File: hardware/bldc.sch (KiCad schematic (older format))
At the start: 7 parts, among them J3 U_OUT, J4 V_OUT, J5 W_OUT, U1 7805

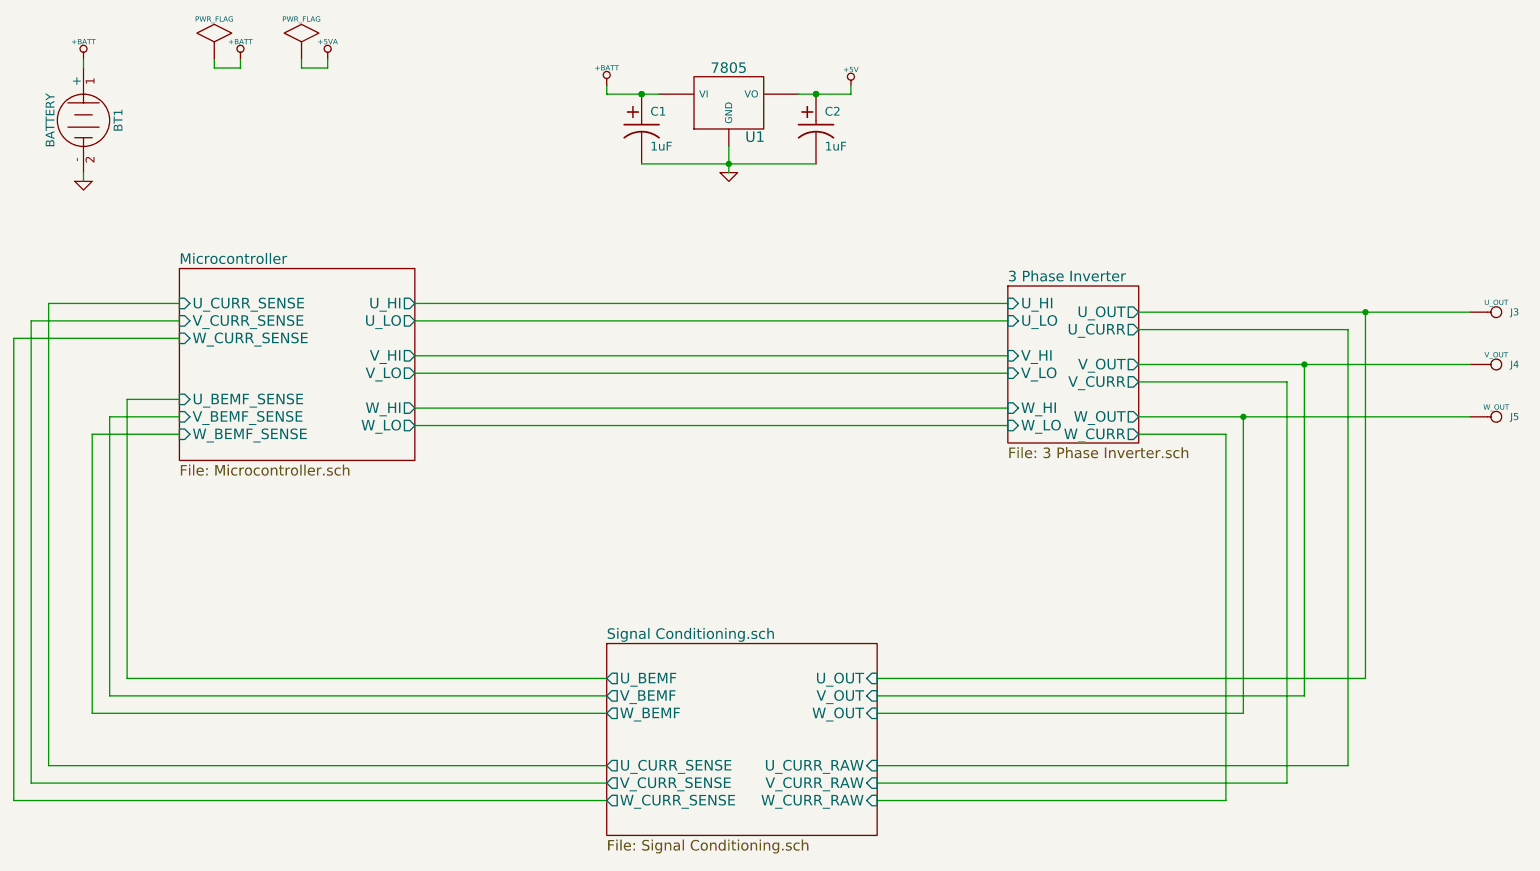
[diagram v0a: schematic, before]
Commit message: Modified the components in the 3 phase inverter
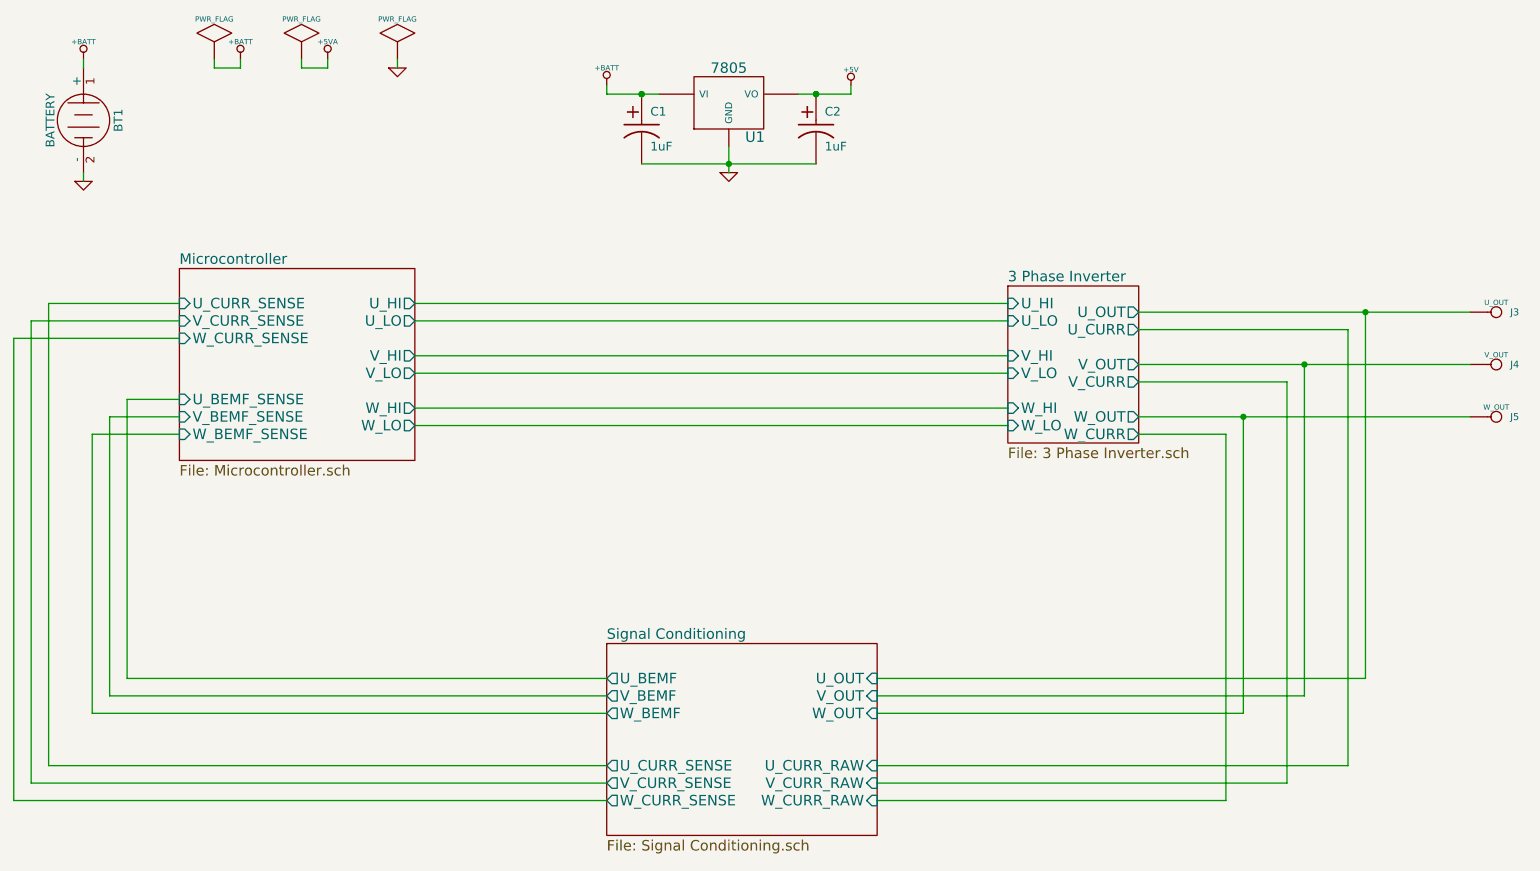
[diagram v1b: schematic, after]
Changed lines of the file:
@@
-EESchema Schematic File Version 2  date Sun 19 Apr 2015 17:21:43 MST
+EESchema Schematic File Version 2  date Sat 25 Apr 2015 16:01:28 MST
 LIBS:power
 LIBS:device
@@
 Sheet 1 4
 Title "BLDC Controller"
-Date "19 apr 2015"
+Date "25 apr 2015"
 Rev "1"
 Comp ""
@@
 $EndDescr
 Wire Wire Line
-	2800 850  2800 900
-Wire Wire Line
-	2800 900  2950 900
-Wire Wire Line
-	2950 900  2950 850
-Wire Wire Line
-	1550 1500 1550 1550
+	3350 900  3350 850
+Wire Wire Line
+	2450 850  2450 900
+Wire Wire Line
+	2450 900  2300 900
+Wire Wire Line
+	2300 900  2300 850
+Wire Wire Line
+	1550 900  1550 850
+Connection ~ 8550 2600
+Wire Wire Line
+	7600 2600 9500 2600
+Wire Wire Line
+	4550 4900 1350 4900
+Wire Wire Line
+	4550 5000 1250 5000
+Wire Wire Line
+	1250 5000 1250 2350
+Wire Wire Line
+	1250 2350 2100 2350
+Wire Wire Line
+	4550 4600 1600 4600
+Wire Wire Line
+	1600 4600 1600 3000
+Wire Wire Line
+	1600 3000 2100 3000
+Wire Wire Line
+	2100 2800 1800 2800
+Wire Wire Line
+	1800 2800 1800 4400
+Wire Wire Line
+	1800 4400 4550 4400
+Wire Wire Line
+	6100 4600 8200 4600
+Wire Wire Line
+	8200 4600 8200 2900
+Wire Wire Line
+	6100 4500 8550 4500
+Wire Wire Line
+	8550 4500 8550 2600
+Wire Wire Line
+	6100 4400 8900 4400
+Wire Wire Line
+	8900 4400 8900 2300
+Wire Wire Line
+	6850 2850 3450 2850
+Wire Wire Line
+	6850 2550 3450 2550
+Wire Wire Line
+	6850 2250 3450 2250
+Connection ~ 5250 1450
+Wire Wire Line
+	5750 1450 4750 1450
+Wire Wire Line
+	5950 1000 5950 1050
+Wire Wire Line
+	5950 1050 5650 1050
+Wire Wire Line
+	4850 1050 4550 1050
+Wire Wire Line
+	4550 1050 4550 1000
+Wire Wire Line
+	5250 1500 5250 1350
+Wire Wire Line
+	3450 2350 6850 2350
+Wire Wire Line
+	3450 2650 6850 2650
+Wire Wire Line
+	3450 2950 6850 2950
+Wire Wire Line
+	7600 2400 8800 2400
+Wire Wire Line
+	8800 2400 8800 4900
+Wire Wire Line
+	8800 4900 6100 4900
+Wire Wire Line
+	7600 2700 8450 2700
+Wire Wire Line
+	8450 2700 8450 5000
+Wire Wire Line
+	8450 5000 6100 5000
+Wire Wire Line
+	7600 3000 8100 3000
+Wire Wire Line
+	8100 3000 8100 5100
+Wire Wire Line
+	8100 5100 6100 5100
+Wire Wire Line
+	4550 4500 1700 4500
+Wire Wire Line
+	1700 4500 1700 2900
+Wire Wire Line
+	1700 2900 2100 2900
+Wire Wire Line
+	1350 4900 1350 2250
+Wire Wire Line
+	1350 2250 2100 2250
+Wire Wire Line
+	4550 5100 1150 5100
+Wire Wire Line
+	1150 5100 1150 2450
+Wire Wire Line
+	1150 2450 2100 2450
+Wire Wire Line
+	7600 2300 9500 2300
+Connection ~ 8900 2300
+Wire Wire Line
+	7600 2900 9500 2900
+Connection ~ 8200 2900
+Connection ~ 4750 1050
+Connection ~ 4750 1050
 Connection ~ 5750 1050
 Connection ~ 5750 1050
-Connection ~ 4750 1050
-Connection ~ 4750 1050
-Connection ~ 8200 2900
-Wire Wire Line
-	7600 2900 9500 2900
-Connection ~ 8900 2300
-Wire Wire Line
-	7600 2300 9500 2300
-Wire Wire Line
-	2100 2450 1150 2450
-Wire Wire Line
-	1150 2450 1150 5100
-Wire Wire Line
-	1150 5100 4550 5100
-Wire Wire Line
-	2100 2250 1350 2250
-Wire Wire Line
-	1350 2250 1350 4900
-Wire Wire Line
-	2100 2900 1700 2900
-Wire Wire Line
-	1700 2900 1700 4500
-Wire Wire Line
-	1700 4500 4550 4500
-Wire Wire Line
-	6100 5100 8100 5100
-Wire Wire Line
-	8100 5100 8100 3000
-Wire Wire Line
-	8100 3000 7600 3000
-Wire Wire Line
-	6100 5000 8450 5000
-Wire Wire Line
-	8450 5000 8450 2700
-Wire Wire Line
-	8450 2700 7600 2700
-Wire Wire Line
-	6100 4900 8800 4900
-Wire Wire Line
-	8800 4900 8800 2400
-Wire Wire Line
-	8800 2400 7600 2400
-Wire Wire Line
-	3450 2950 6850 2950
-Wire Wire Line
-	3450 2650 6850 2650
-Wire Wire Line
-	3450 2350 6850 2350
-Wire Wire Line
-	5250 1500 5250 1350
-Wire Wire Line
-	4550 1000 4550 1050
-Wire Wire Line
-	4550 1050 4850 1050
-Wire Wire Line
-	5650 1050 5950 1050
-Wire Wire Line
-	5950 1050 5950 1000
-Wire Wire Line
-	5750 1450 4750 1450
-Connection ~ 5250 1450
-Wire Wire Line
-	6850 2250 3450 2250
-Wire Wire Line
-	6850 2550 3450 2550
-Wire Wire Line
-	6850 2850 3450 2850
-Wire Wire Line
-	8900 2300 8900 4400
-Wire Wire Line
-	8900 4400 6100 4400
-Wire Wire Line
-	8550 2600 8550 4500
-Wire Wire Line
-	8550 4500 6100 4500
-Wire Wire Line
-	8200 2900 8200 4600
-Wire Wire Line
-	8200 4600 6100 4600
-Wire Wire Line
-	4550 4400 1800 4400
-Wire Wire Line
-	1800 4400 1800 2800
-Wire Wire Line
-	1800 2800 2100 2800
-Wire Wire Line
-	2100 3000 1600 3000
-Wire Wire Line
-	1600 3000 1600 4600
-Wire Wire Line
-	1600 4600 4550 4600
-Wire Wire Line
-	2100 2350 1250 2350
-Wire Wire Line
-	1250 2350 1250 5000
-Wire Wire Line
-	1250 5000 4550 5000
-Wire Wire Line
-	1350 4900 4550 4900
-Wire Wire Line
-	7600 2600 9500 2600
-Connection ~ 8550 2600
-Wire Wire Line
-	1550 900  1550 850
-Wire Wire Line
-	2300 850  2300 900
-Wire Wire Line
-	2300 900  2450 900
-Wire Wire Line
-	2450 900  2450 850
-$Comp
-L +5VA #PWR3
+Wire Wire Line
+	1550 1500 1550 1550
+Wire Wire Line
+	2950 850  2950 900
+Wire Wire Line
+	2950 900  2800 900
+Wire Wire Line
+	2800 900  2800 850
+$Comp
+L GND #PWR01
+U 1 1 553C10DF
+P 3350 900
+F 0 "#PWR01" H 3350 900 30  0001 C CNN
+F 1 "GND" H 3350 830 30  0001 C CNN
+	1    3350 900
+	1    0    0    -1
+$EndComp
+$Comp
+L PWR_FLAG #FLG02
+U 1 1 553C10DA
+P 3350 850
+F 0 "#FLG02" H 3350 1120 30  0001 C CNN
+F 1 "PWR_FLAG" H 3350 1080 30  0000 C CNN
+	1    3350 850
+	1    0    0    -1
+$EndComp
+$Comp
+L +5VA #PWR03
 U 1 1 55343C4A
 P 2950 850
-F 0 "#PWR3" H 2950 980 20  0001 C CNN
+F 0 "#PWR03" H 2950 980 20  0001 C CNN
 F 1 "+5VA" H 2950 950 30  0000 C CNN
 	1    2950 850
@@
 $EndComp
 $Comp
-L PWR_FLAG #FLG2
+L PWR_FLAG #FLG04
 U 1 1 55343C3C
 P 2800 850
-F 0 "#FLG2" H 2800 1120 30  0001 C CNN
+F 0 "#FLG04" H 2800 1120 30  0001 C CNN
 F 1 "PWR_FLAG" H 2800 1080 30  0000 C CNN
 	1    2800 850
@@
 $EndComp
 $Comp
-L PWR_FLAG #FLG1
+L PWR_FLAG #FLG05
 U 1 1 55343C2E
 P 2300 850
-F 0 "#FLG1" H 2300 1120 30  0001 C CNN
+F 0 "#FLG05" H 2300 1120 30  0001 C CNN
 F 1 "PWR_FLAG" H 2300 1080 30  0000 C CNN
 	1    2300 850
@@
 $EndComp
 $Comp
-L +BATT #PWR2
+L +BATT #PWR06
 U 1 1 55343C22
 P 2450 850
-F 0 "#PWR2" H 2450 800 20  0001 C CNN
+F 0 "#PWR06" H 2450 800 20  0001 C CNN
 F 1 "+BATT" H 2450 950 30  0000 C CNN
 	1    2450 850
@@
 $EndComp
 $Comp
-L +BATT #PWR1
+L +BATT #PWR07
 U 1 1 55340DA2
 P 1550 850
-F 0 "#PWR1" H 1550 800 20  0001 C CNN
+F 0 "#PWR07" H 1550 800 20  0001 C CNN
 F 1 "+BATT" H 1550 950 30  0000 C CNN
 	1    1550 850
@@
 $EndComp
 $Comp
-L GND #PWR7
+L GND #PWR08
 U 1 1 55340D98
 P 1550 1550
-F 0 "#PWR7" H 1550 1550 30  0001 C CNN
+F 0 "#PWR08" H 1550 1550 30  0001 C CNN
 F 1 "GND" H 1550 1480 30  0001 C CNN
 	1    1550 1550
@@
 S 4550 4200 1550 1100
 U 5533F799
-F0 "Signal Conditioning.sch" 60
+F0 "Signal Conditioning" 60
 F1 "Signal Conditioning.sch" 60
 F2 "U_CURR_SENSE" O L 4550 4900 60
@@
 $EndSheet
 $Comp
-L GND #PWR6
+L GND #PWR09
 U 1 1 5533EF79
 P 5250 1500
-F 0 "#PWR6" H 5250 1500 30  0001 C CNN
+F 0 "#PWR09" H 5250 1500 30  0001 C CNN
 F 1 "GND" H 5250 1430 30  0001 C CNN
 	1    5250 1500
@@
 $EndComp
 $Comp
-L +BATT #PWR4
+L +BATT #PWR010
 U 1 1 5533EF2A
 P 4550 1000
-F 0 "#PWR4" H 4550 950 20  0001 C CNN
+F 0 "#PWR010" H 4550 950 20  0001 C CNN
 F 1 "+BATT" H 4550 1100 30  0000 C CNN
 	1    4550 1000
@@
 $EndComp
 $Comp
-L +5V #PWR5
+L +5V #PWR011
 U 1 1 5533EF24
 P 5950 1000
-F 0 "#PWR5" H 5950 1090 20  0001 C CNN
+F 0 "#PWR011" H 5950 1090 20  0001 C CNN
 F 1 "+5V" H 5950 1090 30  0000 C CNN
 	1    5950 1000

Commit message: Updated the Part number and footprints for most components
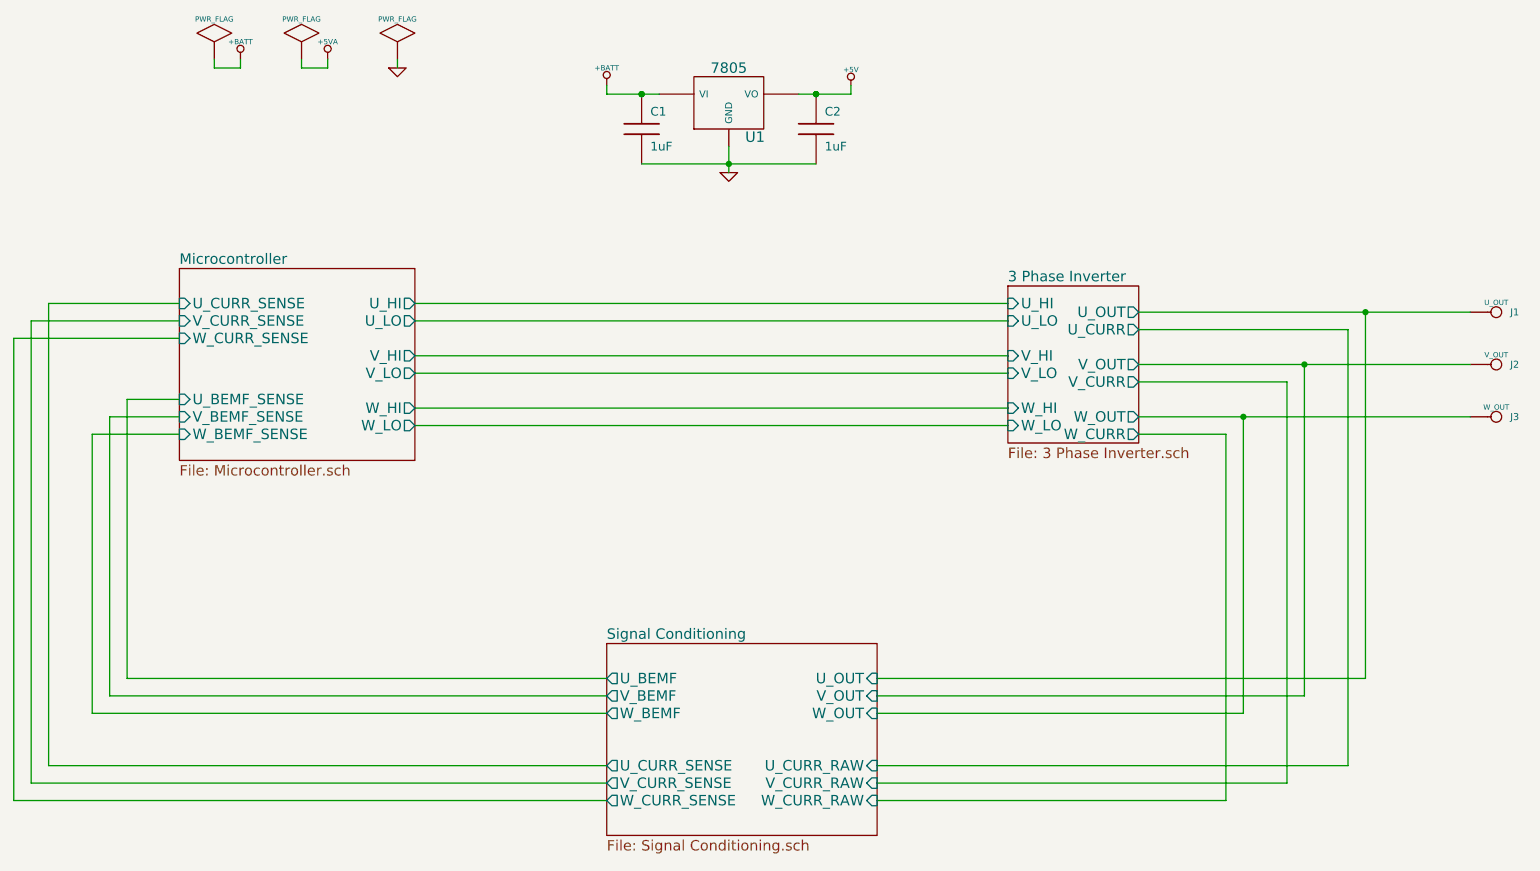
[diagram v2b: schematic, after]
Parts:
- removed BT1: BATTERY, symbol BATTERY
- removed C1, C2: 1uF, symbol CP1
- added C1, C2: 1uF, 0805, symbol C
- U1: footprint (none) -> TO-92; Digikey P/N (none) -> AS78L05ZTR-E1DICT-ND; Mfg P/N (none) -> AS78L05ZTR-E1; Mouser P/N (none) -> 621-AS78L05ZTR-E1
- renumbered J3 to J1, J4 to J2, J5 to J3
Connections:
- net +5V: now also C2.1
- net +BATT: now also C1.1
- net GND: now also C1.2, C2.2
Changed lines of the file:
@@
-EESchema Schematic File Version 2  date Sat 25 Apr 2015 16:01:28 MST
+EESchema Schematic File Version 2  date Sat 25 Apr 2015 17:46:38 MST
 LIBS:power
 LIBS:device
@@
 Sheet 1 4
 Title "BLDC Controller"
-Date "25 apr 2015"
+Date "26 apr 2015"
 Rev "1"
 Comp ""
@@
 Comment4 ""
 $EndDescr
+$Comp
+L C C2
+U 1 1 553C2309
+P 5750 1250
+F 0 "C2" H 5800 1350 50  0000 L CNN
+F 1 "1uF" H 5800 1150 50  0000 L CNN
+F 2 "0805" H 5750 1250 60  0001 C CNN
+F 4 "CL21F105ZBFNNNE" H 5750 1250 60  0001 C CNN "Mfg P/N"
+F 5 "1276-3010-1-ND" H 5750 1250 60  0001 C CNN "Digikey P/N"
+	1    5750 1250
+	1    0    0    -1
+$EndComp
+$Comp
+L C C1
+U 1 1 553C1EAB
+P 4750 1250
+F 0 "C1" H 4800 1350 50  0000 L CNN
+F 1 "1uF" H 4800 1150 50  0000 L CNN
+F 2 "0805" H 4750 1250 60  0001 C CNN
+F 4 "CL21F105ZBFNNNE" H 4750 1250 60  0001 C CNN "Mfg P/N"
+F 5 "1276-3010-1-ND" H 4750 1250 60  0001 C CNN "Digikey P/N"
+	1    4750 1250
+	1    0    0    -1
+$EndComp
 Wire Wire Line
 	3350 900  3350 850
@@
 Wire Wire Line
 	2300 900  2300 850
-Wire Wire Line
-	1550 900  1550 850
 Connection ~ 8550 2600
 Wire Wire Line
@@
 Connection ~ 5750 1050
 Wire Wire Line
-	1550 1500 1550 1550
-Wire Wire Line
 	2950 850  2950 900
 Wire Wire Line
@@
 	2800 900  2800 850
 $Comp
-L GND #PWR01
+L GND #PWR3
 U 1 1 553C10DF
 P 3350 900
-F 0 "#PWR01" H 3350 900 30  0001 C CNN
+F 0 "#PWR3" H 3350 900 30  0001 C CNN
 F 1 "GND" H 3350 830 30  0001 C CNN
 	1    3350 900
@@
 $EndComp
 $Comp
-L PWR_FLAG #FLG02
+L PWR_FLAG #FLG3
 U 1 1 553C10DA
 P 3350 850
-F 0 "#FLG02" H 3350 1120 30  0001 C CNN
+F 0 "#FLG3" H 3350 1120 30  0001 C CNN
 F 1 "PWR_FLAG" H 3350 1080 30  0000 C CNN
 	1    3350 850
@@
 $EndComp
 $Comp
-L +5VA #PWR03
+L +5VA #PWR2
 U 1 1 55343C4A
 P 2950 850
-F 0 "#PWR03" H 2950 980 20  0001 C CNN
+F 0 "#PWR2" H 2950 980 20  0001 C CNN
 F 1 "+5VA" H 2950 950 30  0000 C CNN
 	1    2950 850
@@
 $EndComp
 $Comp
-L PWR_FLAG #FLG04
+L PWR_FLAG #FLG2
 U 1 1 55343C3C
 P 2800 850
-F 0 "#FLG04" H 2800 1120 30  0001 C CNN
+F 0 "#FLG2" H 2800 1120 30  0001 C CNN
 F 1 "PWR_FLAG" H 2800 1080 30  0000 C CNN
 	1    2800 850
@@
 $EndComp
 $Comp
-L PWR_FLAG #FLG05
+L PWR_FLAG #FLG1
 U 1 1 55343C2E
 P 2300 850
-F 0 "#FLG05" H 2300 1120 30  0001 C CNN
+F 0 "#FLG1" H 2300 1120 30  0001 C CNN
 F 1 "PWR_FLAG" H 2300 1080 30  0000 C CNN
 	1    2300 850
@@
 $EndComp
 $Comp
-L +BATT #PWR06
+L +BATT #PWR1
 U 1 1 55343C22
 P 2450 850
-F 0 "#PWR06" H 2450 800 20  0001 C CNN
+F 0 "#PWR1" H 2450 800 20  0001 C CNN
 F 1 "+BATT" H 2450 950 30  0000 C CNN
 	1    2450 850
@@
 $EndComp
 $Comp
-L BATTERY BT1
-U 1 1 5534389A
-P 1550 1200
-F 0 "BT1" H 1550 1400 50  0000 C CNN
-F 1 "BATTERY" H 1550 1010 50  0000 C CNN
-	1    1550 1200
-	0    1    1    0
-$EndComp
-$Comp
-L +BATT #PWR07
-U 1 1 55340DA2
-P 1550 850
-F 0 "#PWR07" H 1550 800 20  0001 C CNN
-F 1 "+BATT" H 1550 950 30  0000 C CNN
-	1    1550 850
-	1    0    0    -1
-$EndComp
-$Comp
-L GND #PWR08
-U 1 1 55340D98
-P 1550 1550
-F 0 "#PWR08" H 1550 1550 30  0001 C CNN
-F 1 "GND" H 1550 1480 30  0001 C CNN
-	1    1550 1550
-	1    0    0    -1
-$EndComp
-$Comp
-L CONN_1 J5
+L CONN_1 J3
 U 1 1 55340D36
 P 9650 2900
-F 0 "J5" H 9730 2900 40  0000 L CNN
+F 0 "J3" H 9730 2900 40  0000 L CNN
 F 1 "W_OUT" H 9650 2955 30  0000 C CNN
 	1    9650 2900
@@
 $EndComp
 $Comp
-L CONN_1 J4
+L CONN_1 J2
 U 1 1 55340D33
 P 9650 2600
-F 0 "J4" H 9730 2600 40  0000 L CNN
+F 0 "J2" H 9730 2600 40  0000 L CNN
 F 1 "V_OUT" H 9650 2655 30  0000 C CNN
 	1    9650 2600
@@
 $EndComp
 $Comp
-L CONN_1 J3
+L CONN_1 J1
 U 1 1 55340D0A
 P 9650 2300
-F 0 "J3" H 9730 2300 40  0000 L CNN
+F 0 "J1" H 9730 2300 40  0000 L CNN
 F 1 "U_OUT" H 9650 2355 30  0000 C CNN
 	1    9650 2300
@@
 $EndSheet
 $Comp
-L GND #PWR09
+L GND #PWR5
 U 1 1 5533EF79
 P 5250 1500
-F 0 "#PWR09" H 5250 1500 30  0001 C CNN
+F 0 "#PWR5" H 5250 1500 30  0001 C CNN
 F 1 "GND" H 5250 1430 30  0001 C CNN
 	1    5250 1500
@@
 $EndComp
 $Comp
-L +BATT #PWR010
+L +BATT #PWR4
 U 1 1 5533EF2A
 P 4550 1000
-F 0 "#PWR010" H 4550 950 20  0001 C CNN
+F 0 "#PWR4" H 4550 950 20  0001 C CNN
 F 1 "+BATT" H 4550 1100 30  0000 C CNN
 	1    4550 1000
@@
 $EndComp
 $Comp
-L +5V #PWR011
+L +5V #PWR6
 U 1 1 5533EF24
 P 5950 1000
-F 0 "#PWR011" H 5950 1090 20  0001 C CNN
+F 0 "#PWR6" H 5950 1090 20  0001 C CNN
 F 1 "+5V" H 5950 1090 30  0000 C CNN
 	1    5950 1000
-	1    0    0    -1
-$EndComp
-$Comp
-L CP1 C1
-U 1 1 5533EF14
-P 4750 1250
-F 0 "C1" H 4800 1350 50  0000 L CNN
-F 1 "1uF" H 4800 1150 50  0000 L CNN
-	1    4750 1250
-	1    0    0    -1
-$EndComp
-$Comp
-L CP1 C2
-U 1 1 5533EF10
-P 5750 1250
-F 0 "C2" H 5800 1350 50  0000 L CNN
-F 1 "1uF" H 5800 1150 50  0000 L CNN
-	1    5750 1250
 	1    0    0    -1
 $EndComp
@@
 F 0 "U1" H 5400 904 60  0000 C CNN
 F 1 "7805" H 5250 1300 60  0000 C CNN
+F 2 "TO-92" H 5250 1100 60  0001 C CNN
+F 4 "AS78L05ZTR-E1" H 5250 1100 60  0001 C CNN "Mfg P/N"
+F 5 "AS78L05ZTR-E1DICT-ND" H 5250 1100 60  0001 C CNN "Digikey P/N"
+F 6 "621-AS78L05ZTR-E1" H 5250 1100 60  0001 C CNN "Mouser P/N"
 	1    5250 1100
 	1    0    0    -1
